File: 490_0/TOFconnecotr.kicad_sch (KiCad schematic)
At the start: 1 part, among them J5 5051102291

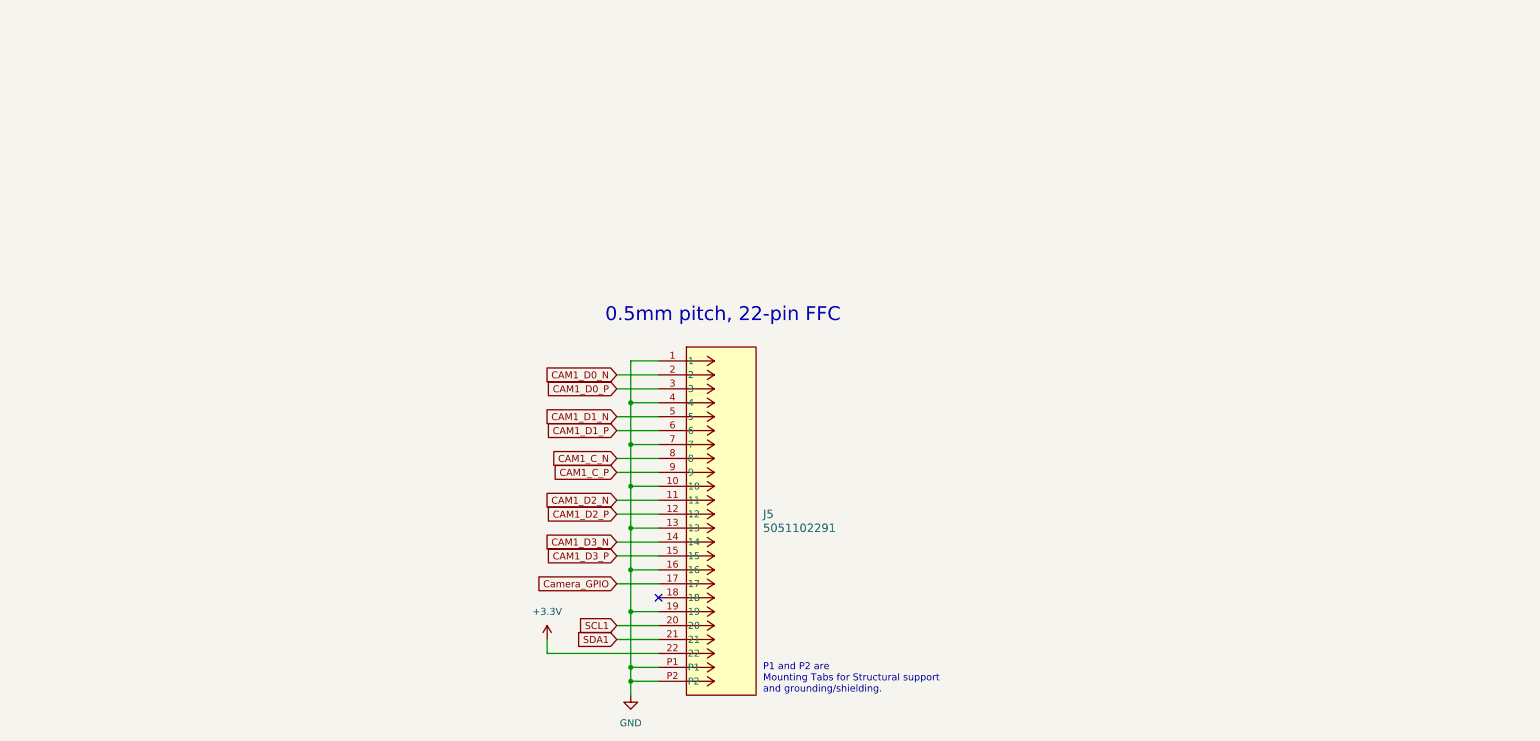
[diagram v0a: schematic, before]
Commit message: Changed PCB block dagram and layout
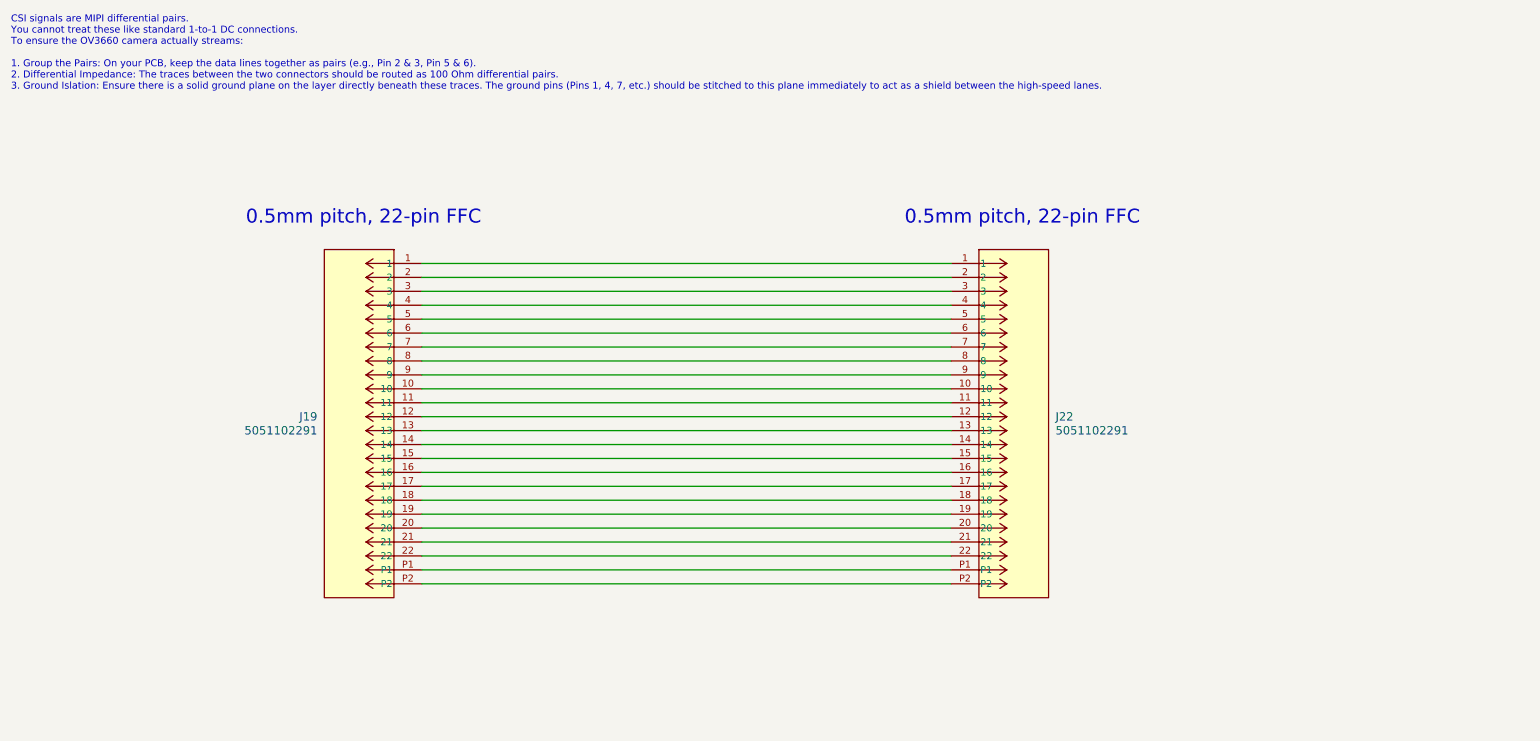
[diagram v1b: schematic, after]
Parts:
- removed J5: 5051102291, CON_5051102291_MOL, symbol capstone_parts:5051102291
- added J19, J22: 5051102291, CON_5051102291_MOL, symbol capstone_parts:5051102291
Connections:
- new net: J19.1, J22.1
- new net: J19.10, J22.10
- new net: J19.11, J22.11
- new net: J19.12, J22.12
- new net: J19.13, J22.13
- new net: J19.14, J22.14
- new net: J19.15, J22.15
- new net: J19.16, J22.16
- new net: J19.17, J22.17
- new net: J19.18, J22.18
- new net: J19.19, J22.19
- new net: J19.2, J22.2
- new net: J19.20, J22.20
- new net: J19.21, J22.21
- new net: J19.22, J22.22
- new net: J19.3, J22.3
- new net: J19.4, J22.4
- new net: J19.5, J22.5
- new net: J19.6, J22.6
- new net: J19.7, J22.7
- new net: J19.8, J22.8
- new net: J19.9, J22.9
- new net: J19.P1, J22.P1
- new net: J19.P2, J22.P2
- no-connect marks 1 -> 0
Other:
- note added: "CSI signals are MIPI differential pairs. You cannot treat these like standard 1-to-1 DC connections. To ensure the OV3660 camera actually streams: 1. Group the Pairs: On your PCB, keep the data lines together as pairs (e.g., Pin 2 & 3, Pin 5 & 6). 2. Differential Impedance: The traces between the two connectors should be routed as 100 Ohm differential pairs. 3. Ground Islation: Ensure there is a 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"
- note removed: "P1 and P2 are Mounting Tabs for Structural support and grounding/shielding."
